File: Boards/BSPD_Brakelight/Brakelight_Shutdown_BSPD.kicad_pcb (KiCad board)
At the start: 2 copper layers, 76.2 x 67.3 mm, 91 parts, among them IC1 ATMEGA16M1, J2 MM_F_RA_20, J3 CONN_02X03, Q1 SSM3K333R, Q2 SSM3K333R, Q3 SSM3K333R, Q6 SSM3K333R, U1 SN74LVC1G08, U101 TPS560430YF, U2 MCP6001, U3 CAN_Transceiver, U4 MCP6001, U5 SN74LVC1G02, U6 SN74LVC1G02, U7 MCP6001, U8 SN74LVC1G32, Y1 Crystal_SMD

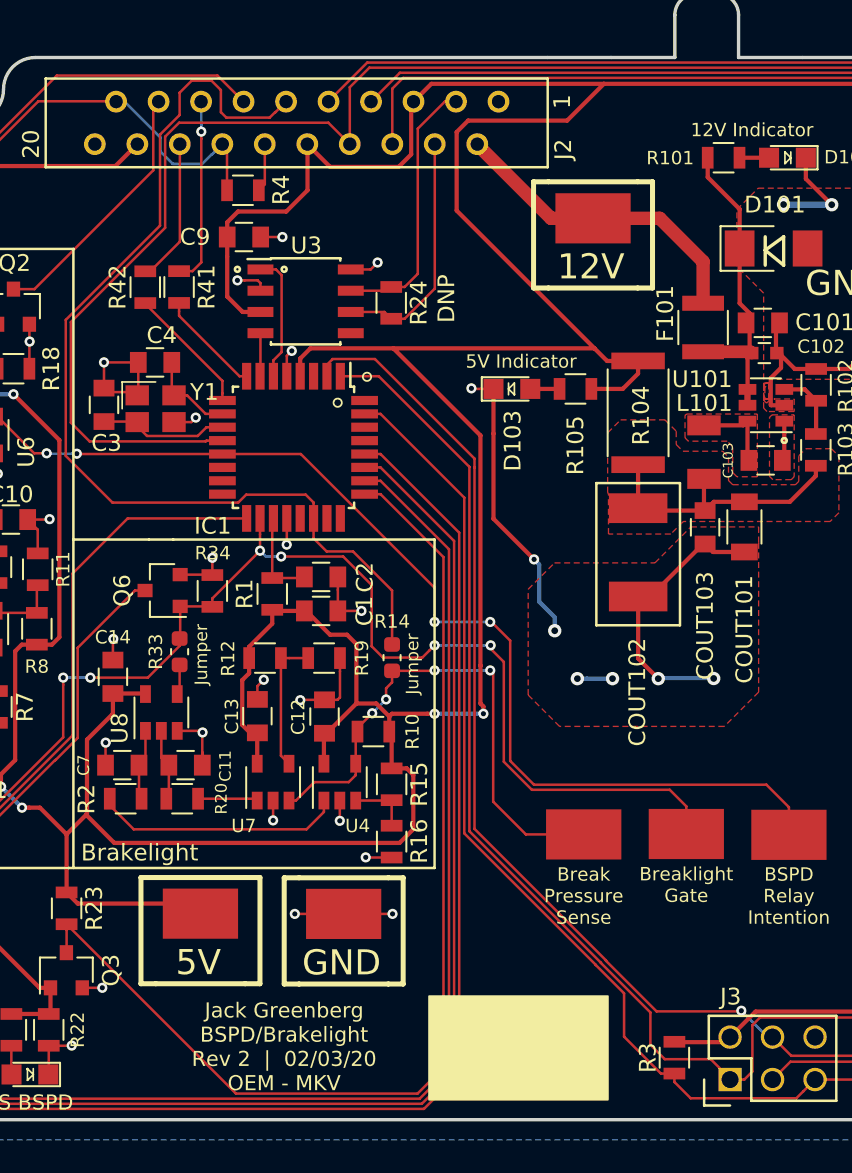
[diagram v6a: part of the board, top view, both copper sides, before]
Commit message: Updated BSPD/Brakelight with Manu's fixes
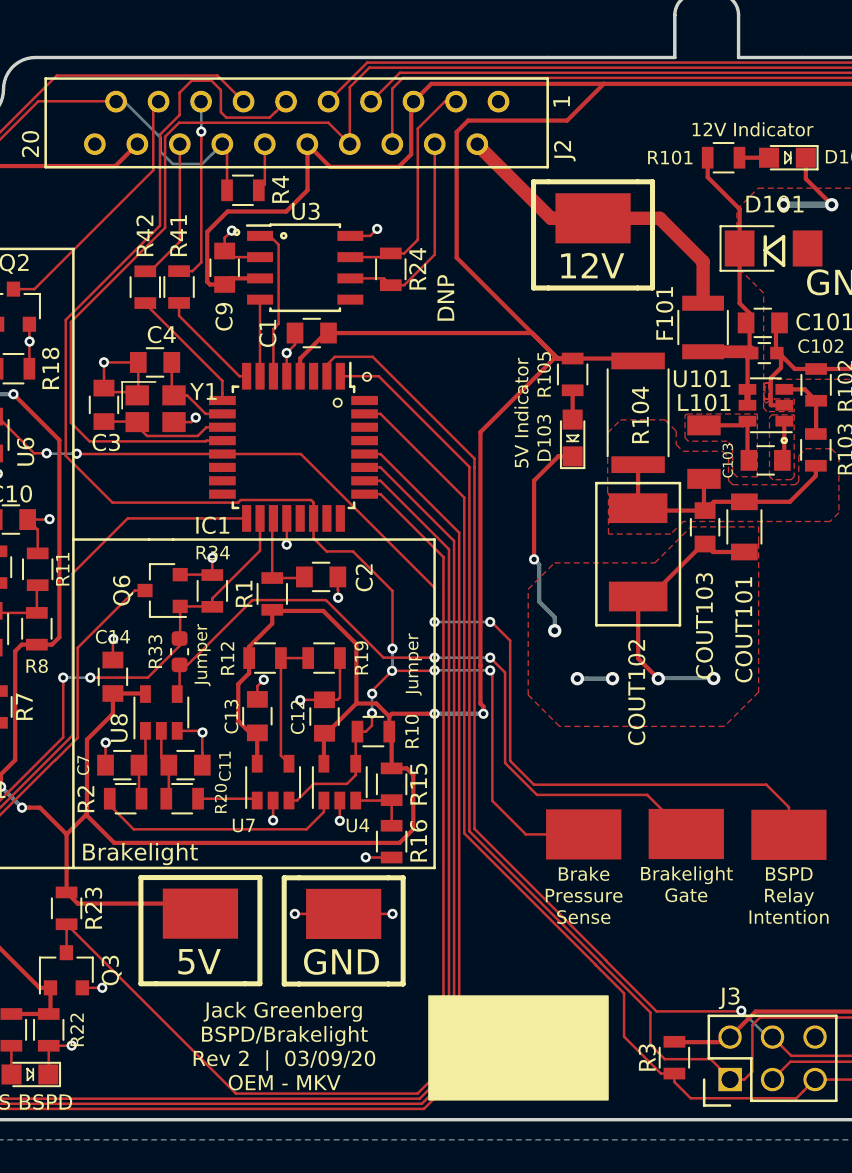
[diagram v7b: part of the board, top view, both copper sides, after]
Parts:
- removed the G*** at (235.9, 97.8)
- removed R14: R_0, footprints:R_0603_1608Metric
- added G***: LOGO, footprints:Olin_Electric_Smaller, B.Cu at (256.6, 91.8)
- moved C1 16.6 mm to (234.5, 56.2), turned to 180 degrees
- moved D103 4.67 mm to (250.1, 62.4), turned to 90 degrees
- moved C9 2.17 mm to (229.3, 52.3), turned to 90 degrees
- moved R24 2.01 mm to (239.2, 52.3)
- moved U3 2.01 mm to (234.1, 52.3)
- moved R105 0.88 mm to (250.1, 58.6), turned to 270 degrees
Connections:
- net /SHUTDOWN_SENSE_BSPD_PIN renamed /~SHUTDOWN_SENSE_BSPD_PIN
- R10 pad 2: Net-(R10-Pad2) -> /BRAKE_PRESSURE_SENSE
- TP1 pad 1: Net-(R10-Pad2) -> /BRAKE_PRESSURE_SENSE
- TP2 pad 1: /BRAKELIGHT_GATE -> Net-(R33-Pad2)
- U4 pad 4: Net-(R10-Pad2) -> /BRAKE_PRESSURE_SENSE
- U7 pad 3: Net-(R10-Pad2) -> /BRAKE_PRESSURE_SENSE
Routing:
- net Net-(R33-Pad2): track 1.80 -> 42.7 mm, vias 0 -> 2
- net /BRAKELIGHT_GATE: track 73.5 -> 33.7 mm, vias 6 -> 2
- net /BRAKE_PRESSURE_SENSE: track 61.0 -> 94.7 mm, vias 0 -> 6
- net Net-(R10-Pad2): track 31.8 -> 0.00 mm, vias 4 -> 0
- net GND: track 141.1 -> 135.6 mm, vias 47 -> 45
- net VCC: track 351.1 -> 348.7 mm
- net /RXCAN: track 2.58 -> 4.61 mm
- net /CAN_LOW: track 14.6 -> 12.6 mm
- net /CAN_HIGH: track 16.1 -> 14.1 mm
- net /TXCAN: track 7.65 -> 9.32 mm
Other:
- board text added: "Brake Pressure Sense"
- board text added: "Brakelight Gate"
- board text added: "Jack Greenberg BSPD/Brakelight Rev 2 | 03/09/20 OEM - MKV"
- board text removed: "Break Pressure Sense"
- board text removed: "Breaklight Gate"
- board text removed: "Jack Greenberg BSPD/Brakelight Rev 2 | 02/03/20 OEM - MKV"
